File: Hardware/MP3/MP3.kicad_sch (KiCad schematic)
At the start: 2 parts, among them J1 Conn_02x20_Odd_Even

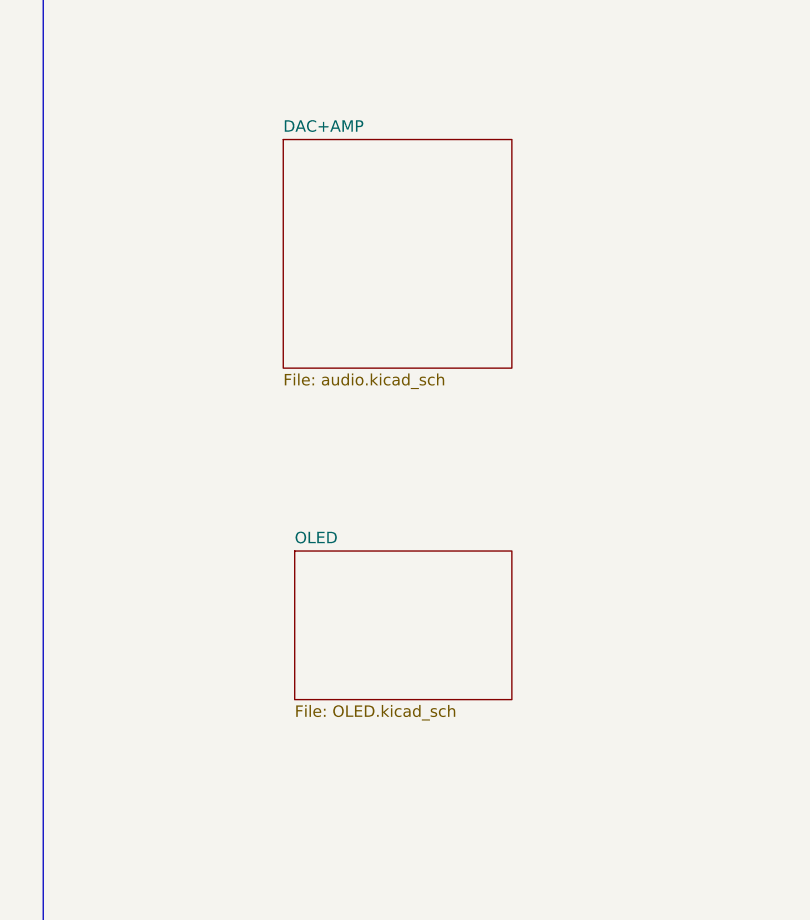
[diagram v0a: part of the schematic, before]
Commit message: feat: Changes to the power circuitry to sort out the regulators (schematic and footprint sorted). Additionally, headphone jack needs to be sorted, both schematic and actual component.
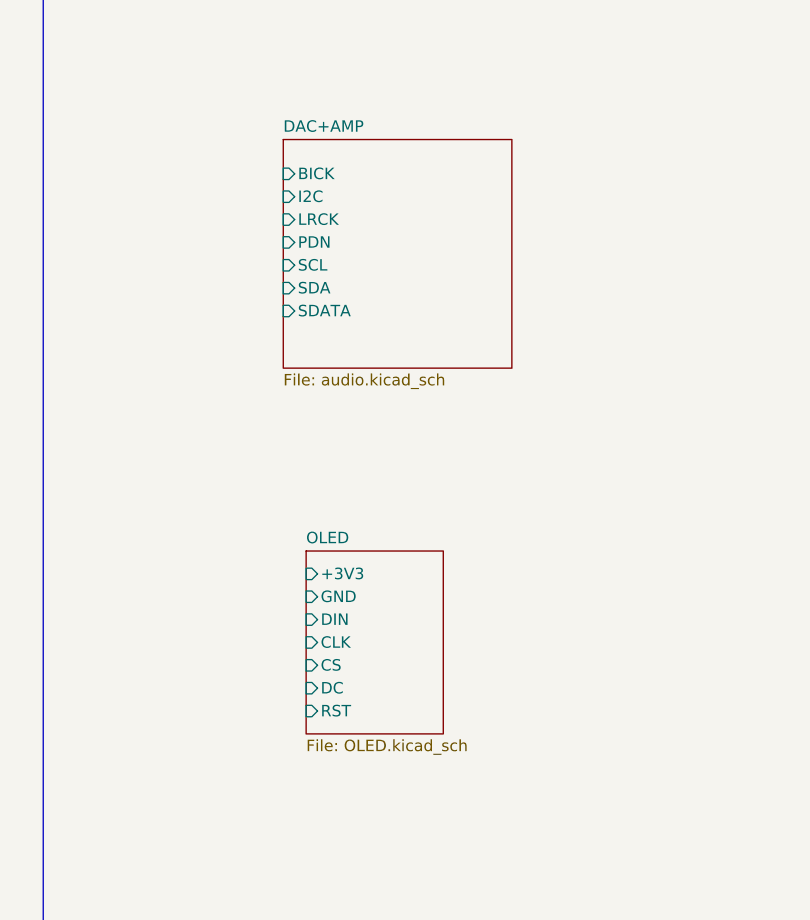
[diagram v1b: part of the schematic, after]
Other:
- sheet DAC+AMP ports: added BICK, I2C, LRCK, PDN, SCL, SDA, SDATA; removed none
- sheet OLED ports: added +3V3, CLK, CS, DC, DIN, GND, RST; removed none
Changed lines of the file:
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@@
+			)
+		)
+		(pin "BICK" input
+			(at 203.2 67.31 180)
+			(effects
+				(font
+					(size 1.27 1.27)
+				)
+				(justify left)
+			)
+		)
+		(pin "I2C" input
+			(at 203.2 69.85 180)
+			(effects
+				(font
+					(size 1.27 1.27)
+				)
+				(justify left)
+			)
+		)
+		(pin "LRCK" input
+			(at 203.2 72.39 180)
+			(effects
+				(font
+					(size 1.27 1.27)
+				)
+				(justify left)
+			)
+		)
+		(pin "PDN" input
+			(at 203.2 74.93 180)
+			(effects
+				(font
+					(size 1.27 1.27)
+				)
+				(justify left)
+			)
+		)
+		(pin "SCL" input
+			(at 203.2 77.47 180)
+			(effects
+				(font
+					(size 1.27 1.27)
+				)
+				(justify left)
+			)
+		)
+		(pin "SDA" input
+			(at 203.2 80.01 180)
+			(effects
+				(font
+					(size 1.27 1.27)
+				)
+				(justify left)
+			)
+		)
+		(pin "SDATA" input
+			(at 203.2 82.55 180)
+			(effects
+				(font
+					(size 1.27 1.27)
+				)
+				(justify left)
 			)
 		)
@@
 	)
 	(sheet
-		(at 204.47 109.22)
-		(size 24.13 16.51)
+		(at 205.74 109.22)
+		(size 15.24 20.32)
 		(exclude_from_sim no)
 		(in_bom yes)
@@
 		)
 		(property "Sheetname" "OLED"
-			(at 204.47 108.5084 0)
+			(at 205.74 108.5084 0)
 			(effects
 				(font
@@
 		)
 		(property "Sheetfile" "OLED.kicad_sch"
-			(at 204.47 126.3146 0)
+			(at 205.74 130.1246 0)
 			(effects
 				(font
@@
 			)
 		)
+		(pin "+3V3" input
+			(at 205.74 111.76 180)
+			(effects
+				(font
+					(size 1.27 1.27)
+				)
+				(justify left)
+			)
+		)
+		(pin "CLK" input
+			(at 205.74 119.38 180)
+			(effects
+				(font
+					(size 1.27 1.27)
+				)
+				(justify left)
+			)
+		)
+		(pin "CS" input
+			(at 205.74 121.92 180)
+			(effects
+				(font
+					(size 1.27 1.27)
+				)
+				(justify left)
+			)
+		)
+		(pin "DC" input
+			(at 205.74 124.46 180)
+			(effects
+				(font
+					(size 1.27 1.27)
+				)
+				(justify left)
+			)
+		)
+		(pin "DIN" input
+			(at 205.74 116.84 180)
+			(effects
+				(font
+					(size 1.27 1.27)
+				)
+				(justify left)
+			)
+		)
+		(pin "GND" input
+			(at 205.74 114.3 180)
+			(effects
+				(font
+					(size 1.27 1.27)
+				)
+				(justify left)
+			)
+		)
+		(pin "RST" input
+			(at 205.74 127 180)
+			(effects
+				(font
+					(size 1.27 1.27)
+				)
+				(justify left)
+			)
+		)
